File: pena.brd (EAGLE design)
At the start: 108.9 x 59.4 mm, 26 parts

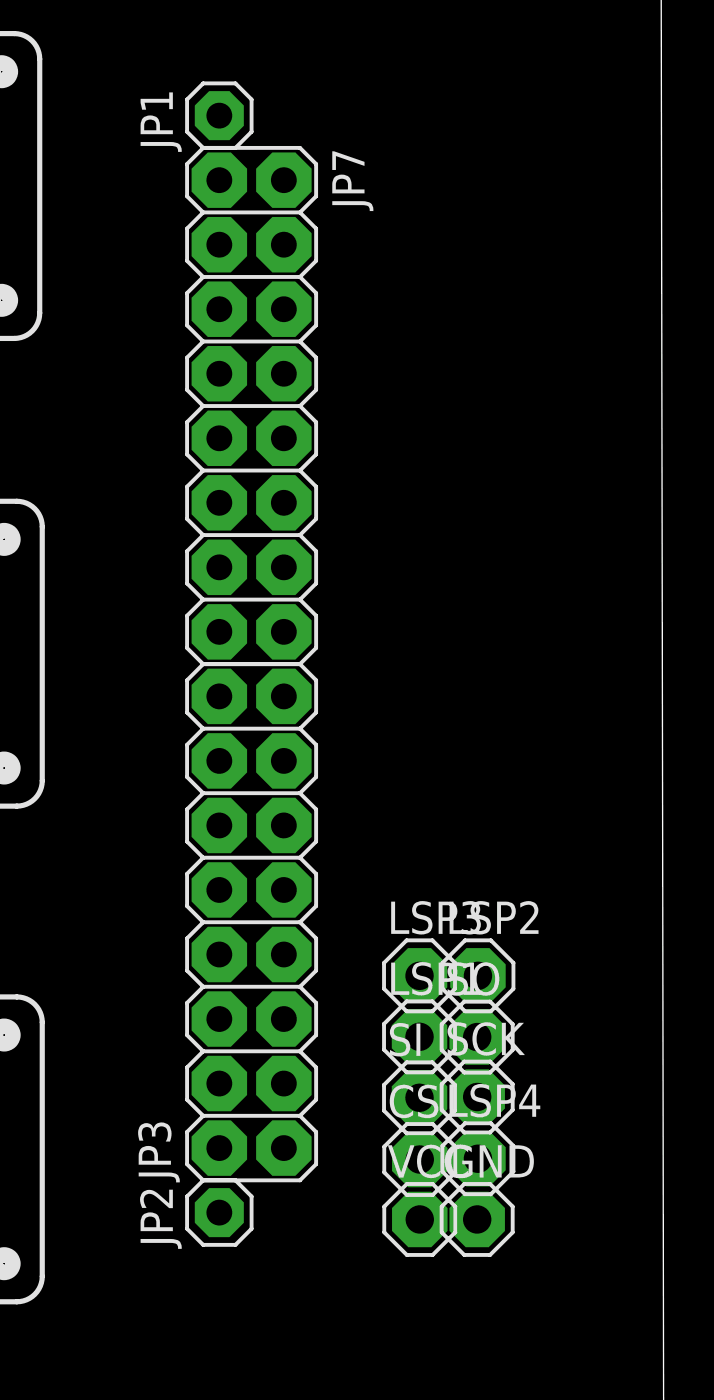
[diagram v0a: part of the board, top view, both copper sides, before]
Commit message: Vaihdettu reikien kokoa.
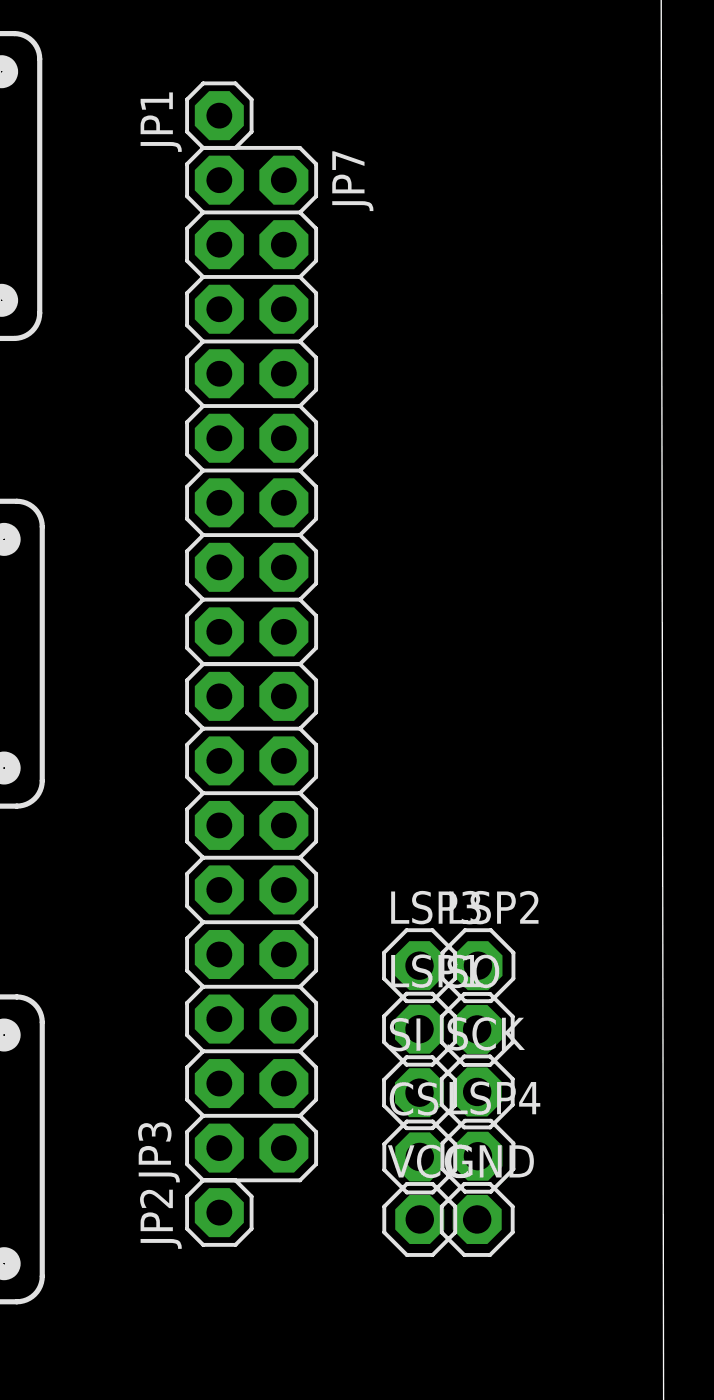
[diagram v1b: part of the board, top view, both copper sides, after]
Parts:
- moved LSP2 0.40 mm to (99.2, 43.4)
- moved LSP3 0.40 mm to (96.9, 43.4)
- moved LSP1 0.30 mm to (96.9, 40.9)
- moved SO 0.30 mm to (99.2, 40.9)
- moved SCK 0.20 mm to (99.2, 38.4)
- moved SI 0.20 mm to (96.9, 38.4)
- moved LSP4 0.10 mm to (99.2, 35.9)
- moved CS 0.10 mm to (96.9, 35.9)
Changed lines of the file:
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@@
 <element name="JP3" library="mega" package="2X08" value="" x="90.29" y="45.11" rot="R90"/>
 <element name="VCC" library="solpad" package="SE11" value="SE11" x="96.91" y="33.41"/>
-<element name="CS" library="solpad" package="SE11" value="SE11" x="96.91" y="35.77"/>
+<element name="CS" library="solpad" package="SE11" value="SE11" x="96.91" y="35.87"/>
 <element name="GND" library="solpad" package="SE11" value="SE11" x="99.17" y="33.41"/>
-<element name="SCK" library="solpad" package="SE11" value="SE11" x="99.17" y="38.23"/>
-<element name="SO" library="solpad" package="SE11" value="SE11" x="99.17" y="40.59"/>
-<element name="SI" library="solpad" package="SE11" value="SE11" x="96.9" y="38.2"/>
-<element name="LSP1" library="solpad" package="SE11" value="SE11" x="96.9" y="40.6"/>
-<element name="LSP2" library="solpad" package="SE11" value="SE11" x="99.2" y="43"/>
-<element name="LSP3" library="solpad" package="SE11" value="SE11" x="96.9" y="43"/>
-<element name="LSP4" library="solpad" package="SE11" value="SE11" x="99.2" y="35.8"/>
+<element name="SCK" library="solpad" package="SE11" value="SE11" x="99.17" y="38.43"/>
+<element name="SO" library="solpad" package="SE11" value="SE11" x="99.17" y="40.89"/>
+<element name="SI" library="solpad" package="SE11" value="SE11" x="96.9" y="38.4"/>
+<element name="LSP1" library="solpad" package="SE11" value="SE11" x="96.9" y="40.9"/>
+<element name="LSP2" library="solpad" package="SE11" value="SE11" x="99.2" y="43.4"/>
+<element name="LSP3" library="solpad" package="SE11" value="SE11" x="96.9" y="43.4"/>
+<element name="LSP4" library="solpad" package="SE11" value="SE11" x="99.2" y="35.9"/>
 </elements>
 <signals>
@@
 <contactref element="JP3" pad="1"/>
 <contactref element="CS" pad="MP"/>
-<wire x1="91.56" y1="36.22" x2="96.91" y2="35.77" width="0" layer="19" extent="1-1"/>
+<wire x1="91.56" y1="36.22" x2="96.91" y2="35.87" width="0" layer="19" extent="1-1"/>
 </signal>
 <signal name="51">
 <contactref element="JP3" pad="3"/>
 <contactref element="SI" pad="MP"/>
-<wire x1="91.56" y1="38.76" x2="96.9" y2="38.2" width="0" layer="19" extent="1-1"/>
+<wire x1="91.56" y1="38.76" x2="96.9" y2="38.4" width="0" layer="19" extent="1-1"/>
 </signal>
 <signal name="49">
@@
 <contactref element="JP3" pad="2"/>
 <contactref element="SCK" pad="MP"/>
-<wire x1="89.02" y1="36.22" x2="99.17" y2="38.23" width="0" layer="19" extent="1-1"/>
+<wire x1="89.02" y1="36.22" x2="99.17" y2="38.43" width="0" layer="19" extent="1-1"/>
 </signal>
 <signal name="50">
 <contactref element="JP3" pad="4"/>
 <contactref element="SO" pad="MP"/>
-<wire x1="89.02" y1="38.76" x2="99.17" y2="40.59" width="0" layer="19" extent="1-1"/>
+<wire x1="89.02" y1="38.76" x2="99.17" y2="40.89" width="0" layer="19" extent="1-1"/>
 </signal>
 <signal name="48">

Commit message: Luotu routet.
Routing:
- net GND: track 0.00 -> 276.6 mm
- net 28: track 0.00 -> 88.0 mm
- net 44: track 0.00 -> 87.0 mm
- net 36: track 0.00 -> 84.8 mm
- net 52: track 0.00 -> 67.0 mm
- net 42: track 0.00 -> 65.8 mm
- net 26: track 0.00 -> 65.7 mm
- net 34: track 0.00 -> 62.5 mm
- net +5V: track 0.00 -> 49.1 mm
- net 24: track 0.00 -> 42.9 mm
- net 40: track 0.00 -> 42.2 mm
- net 32: track 0.00 -> 41.9 mm
- net 50: track 0.00 -> 33.3 mm
- net 38: track 0.00 -> 20.2 mm
- net 22: track 0.00 -> 18.1 mm
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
